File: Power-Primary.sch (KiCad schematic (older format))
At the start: 45 parts, among them J1 HV in, J10 SPARE, J11 SPARE, J2 Dashboard, J3 Telemetry, J4 Motor, J5 MPPT 1, J6 MPPT 2, J7 BPS, J8 Primary Disconn., J9 SPARE, U1 Mean_Well_12V

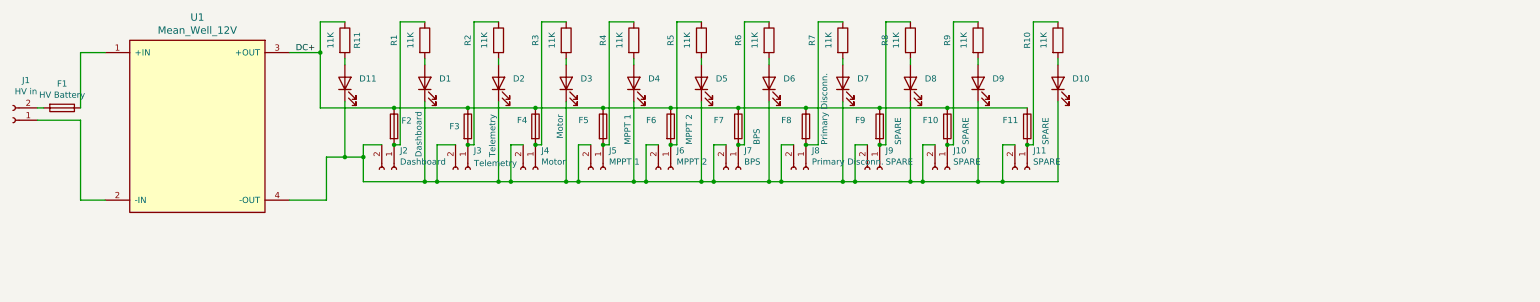
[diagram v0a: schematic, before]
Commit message: Extend design (#1)
* Practice push + changed schematic

* schematic almost done, connection errors

* schematic done, U1 pin 3/4 error

* finished schematic

* finished PCB waiting for edits

* pcb edits

* fixed component spacing

* refilled zones

* completed Hannah's edits

* Sijin's edits, mounting hole and power planes

* Deletes gerbers from this because added to release and adds dimensions

Co-authored-by: Hannahslee14 <hannahslee@utexas.edu>
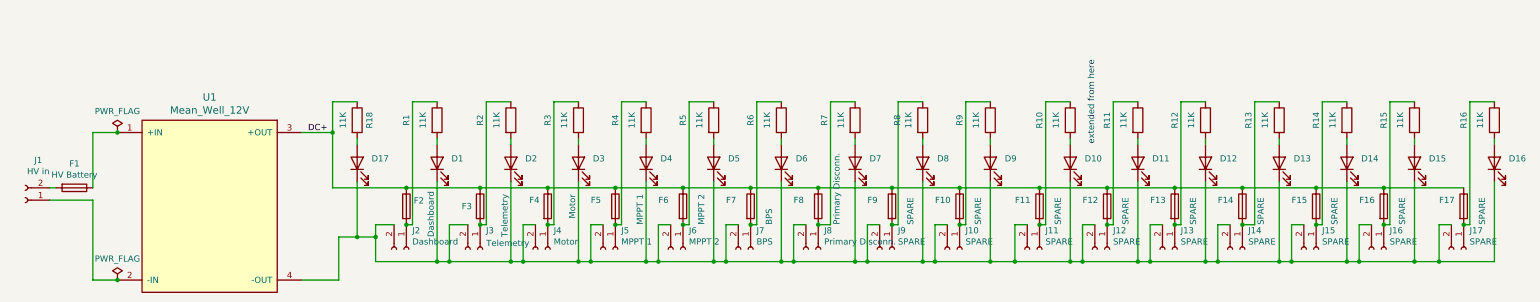
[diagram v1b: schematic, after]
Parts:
- added D11, D12, D13, D14, D15, D16: LED, LED_THT:LED_D3.0mm, symbol Device:LED
- added F12, F13, F14, F15, F16, F17: SPARE, Fuse:Fuseholder_Blade_Mini_Keystone_3568, symbol Device:Fuse
- added J12, J13, J14, J15, J16, J17: SPARE, Connector_Molex:Molex_Micro-Fit_3.0_43650-0215_1x02_P3.00mm_Vertical, symbol Connector:Conn_01x02_Female
- added R11, R12, R13, R14, R15, R16: 11K, Resistor_THT:R_Axial_DIN0204_L3.6mm_D1.6mm_P7.62mm_Horizontal, symbol Device:R
- renumbered D11 to D17, R11 to R18
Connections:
- net DC+: now also F12.1, F13.1, F14.1, F15.1, F16.1, F17.1
- net at D1.1 (K), D10.1 (K), D17.1 (K)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: now also D11.1 (K), D12.1 (K), D13.1 (K), D14.1 (K), D15.1 (K), D16.1 (K), J12.2 (Pin_2), J13.2 (Pin_2), J14.2 (Pin_2), J15.2 (Pin_2), J16.2 (Pin_2), J17.2 (Pin_2)
- new net: F12.2, J12.1 (Pin_1), R11.1
- new net: D11.2 (A), R11.2
- new net: F13.2, J13.1 (Pin_1), R12.1
- new net: D12.2 (A), R12.2
- new net: F15.2, J15.1 (Pin_1), R14.1
- new net: D14.2 (A), R14.2
- new net: F16.2, J16.1 (Pin_1), R15.1
- new net: D15.2 (A), R15.2
- new net: F17.2, J17.1 (Pin_1), R16.1
- new net: D16.2 (A), R16.2
- new net: F14.2, J14.1 (Pin_1), R13.1
- new net: D13.2 (A), R13.2
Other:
- note added: "extended from here"
- moved on the sheet: D1, D10, D17, D2, D3, D4, D5, D6, D7, D8, D9, F1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
